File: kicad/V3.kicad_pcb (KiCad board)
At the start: 2 copper layers, 172.9 x 118.3 mm, 51 parts, among them SW1 Slide_Switch_SPDT_P3mm_10x5x1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

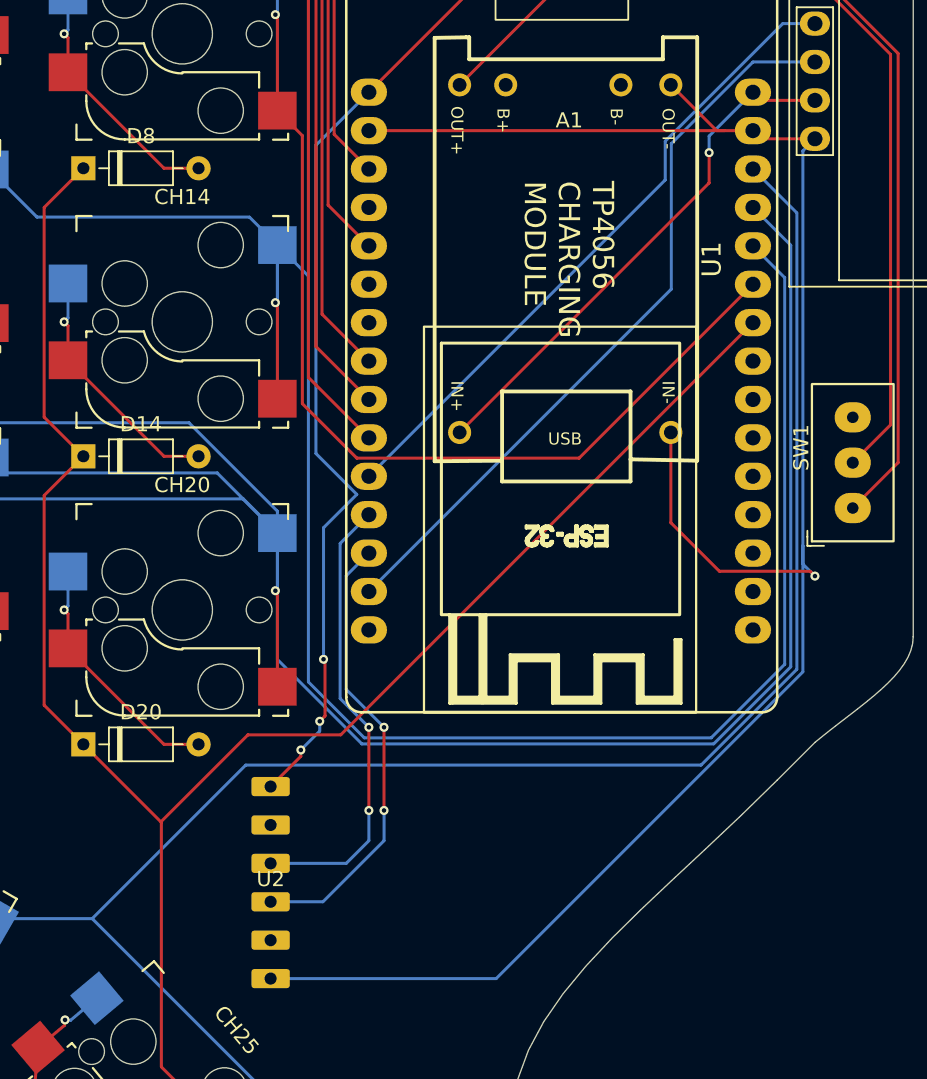
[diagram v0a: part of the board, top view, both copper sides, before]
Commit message: changed uart-hid pinout
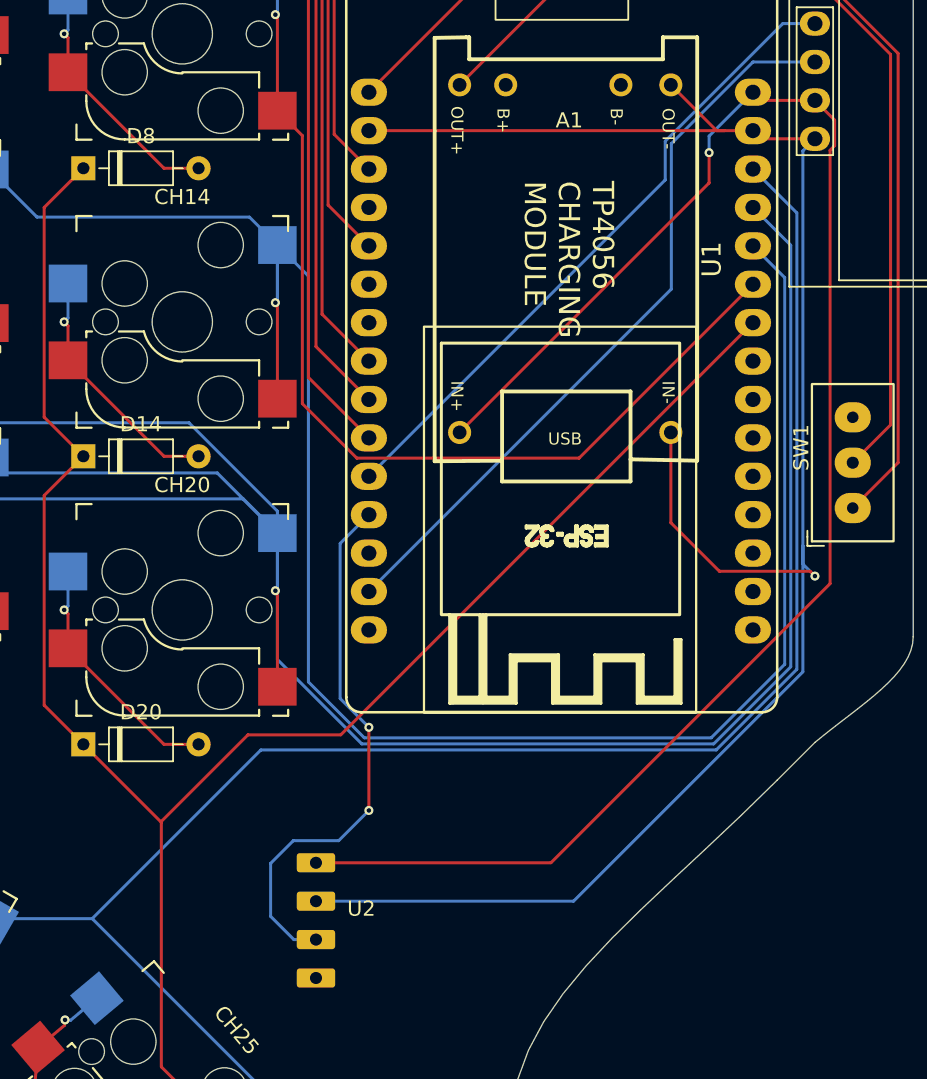
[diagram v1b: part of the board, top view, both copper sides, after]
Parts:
- U2: footprint Library:CH340C_pins -> Library:CH9328
- moved U2 3.63 mm to (194.0, 119.1)
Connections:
- U2 pad 1: -3V3 -> VCC
- U2 pad 2: unconnected-(U2-DTR-Pad2) -> Earth
- U2 pad 4: /TX -> unconnected-(U2-RST-Pad4)
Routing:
- net VCC: track 34.9 -> 109.1 mm
- net -3V3: track 122.3 -> 71.4 mm, vias 3 -> 0
- net /TX: track 29.9 -> 0.00 mm, vias 2 -> 0
- net /RX: track 30.3 -> 36.2 mm
- net Earth: track 133.0 -> 127.9 mm

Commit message: slkscreen
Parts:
- moved U2 7.83 mm to (201.8, 119.2)
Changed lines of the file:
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@@
 		(embedded_fonts no)
 	)
-	(footprint "Library:CH9328"
-		(layer "F.Cu")
-		(at 194 119.08)
-		(property "Reference" "U2"
-			(at 3 -0.58 0)
-			(unlocked yes)
-			(layer "F.SilkS")
-			(effects
-				(font
-					(size 1 1)
-					(thickness 0.1)
-				)
-			)
-		)
-		(property "Value" "~"
-			(at 3 0.92 0)
-			(unlocked yes)
-			(layer "F.Fab")
-			(effects
-				(font
-					(size 1 1)
-					(thickness 0.15)
-				)
-			)
-		)
-		(property "Datasheet" ""
-			(at 0 0 0)
-			(unlocked yes)
-			(layer "F.Fab")
-			(hide yes)
-			(effects
-				(font
-					(size 1 1)
-					(thickness 0.15)
-				)
-			)
-		)
-		(property "Description" ""
-			(at 0 0 0)
-			(unlocked yes)
-			(layer "F.Fab")
-			(hide yes)
-			(effects
-				(font
-					(size 1 1)
-					(thickness 0.15)
-				)
-			)
-		)
-		(sheetname "/")
-		(sheetfile "V3.kicad_sch")
-		(fp_text user "${REFERENCE}"
-			(at 0 2.5 0)
-			(unlocked yes)
-			(layer "F.Fab")
-			(effects
-				(font
-					(size 1 1)
-					(thickness 0.15)
-				)
-			)
-		)
-		(pad "1" thru_hole roundrect
-			(at 0 -3.62)
-			(size 2.54 1.27)
-			(drill 0.8)
-			(layers "*.Cu" "*.Mask")
-			(remove_unused_layers no)
-			(roundrect_rratio 0.15)
-			(net 8 "VCC")
-			(pinfunction "Vcc")
-			(pintype "power_in")
-			(thermal_bridge_angle 45)
-		)
-		(pad "2" thru_hole roundrect
-			(at 0 -1.08)
-			(size 2.54 1.27)
-			(drill 0.8)
-			(layers "*.Cu" "*.Mask")
-			(remove_unused_layers no)
-			(roundrect_rratio 0.15)
-			(net 11 "Earth")
-			(pinfunction "GND")
-			(pintype "power_in")
-			(thermal_bridge_angle 45)
-		)
-		(pad "3" thru_hole roundrect
-			(at 0 1.46)
-			(size 2.54 1.27)
-			(drill 0.8)
-			(layers "*.Cu" "*.Mask")
-			(remove_unused_layers no)
-			(roundrect_rratio 0.15)
-			(net 45 "/RX")
-			(pinfunction "RX")
-			(pintype "input")
-			(thermal_bridge_angle 45)
-		)
-		(pad "4" thru_hole roundrect
-			(at 0 4)
-			(size 2.54 1.27)
-			(drill 0.8)
-			(layers "*.Cu" "*.Mask")
-			(remove_unused_layers no)
-			(roundrect_rratio 0.15)
-			(net 53 "unconnected-(U2-RST-Pad4)")
-			(pinfunction "RST")
-			(pintype "input")
-			(thermal_bridge_angle 45)
-		)
-		(embedded_fonts no)
-	)
 	(footprint "Diode_THT:D_DO-35_SOD27_P7.62mm_Horizontal"
 		(layer "F.Cu")
@@
 		)
 		(embedded_fonts no)
+	)
+	(footprint "Library:CH9328"
+		(layer "F.Cu")
+		(at 201.83262 119.25)
+		(property "Reference" "U2"
+			(at -7.404 -0.7 0)
+			(unlocked yes)
+			(layer "F.SilkS")
+			(effects
+				(font
+					(size 1 1)
+					(thickness 0.1)
+				)
+			)
+		)
+		(property "Value" "~"
+			(at 0 1 0)
+			(unlocked yes)
+			(layer "F.Fab")
+			(effects
+				(font
+					(size 1 1)
+					(thickness 0.15)
+				)
+			)
+		)
+		(property "Datasheet" ""
+			(at 0 0 0)
+			(unlocked yes)
+			(layer "F.Fab")
+			(hide yes)
+			(effects
+				(font
+					(size 1 1)
+					(thickness 0.15)
+				)
+			)
+		)
+		(property "Description" ""
+			(at 0 0 0)
+			(unlocked yes)
+			(layer "F.Fab")
+			(hide yes)
+			(effects
+				(font
+					(size 1 1)
+					(thickness 0.15)
+				)
+			)
+		)
+		(sheetname "/")
+		(sheetfile "V3.kicad_sch")
+		(fp_line
+			(start -10.26124 -10.5)
+			(end -10.26124 10)
+			(stroke
+				(width 0.1)
+				(type default)
+			)
+			(layer "F.SilkS")
+		)
+		(fp_line
+			(start -10.26124 -10.5)
+			(end 15.096 -10.5)
+			(stroke
+				(width 0.1)
+				(type default)
+			)
+			(layer "F.SilkS")
+		)
+		(fp_line
+			(start -10.26124 10)
+			(end 15.096 10)
+			(stroke
+				(width 0.1)
+				(type default)
+			)
+			(layer "F.SilkS")
+		)
+		(fp_line
+			(start 15.096 -10.5)
+			(end 15.096 10)
+			(stroke
+				(width 0.1)
+				(type default)
+			)
+			(layer "F.SilkS")
+		)
+		(fp_rect
+			(start 9.096 -4.5)
+			(end 16.596 4)
+			(stroke
+				(width 0.1)
+				(type default)
+			)
+			(fill no)
+			(layer "F.SilkS")
+		)
+		(fp_text user "Usb"
+			(at 12.096 -2.5 270)
+			(unlocked yes)
+			(layer "F.SilkS")
+			(effects
+				(font
+					(size 1.5 1.5)
+					(thickness 0.3)
+					(bold yes)
+				)
+				(justify left bottom)
+			)
+		)
+		(fp_text user "${REFERENCE}"
+			(at 0 2.5 0)
+			(unlocked yes)
+			(layer "F.Fab")
+			(effects
+				(font
+					(size 1 1)
+					(thickness 0.15)
+				)
+			)
+		)
+		(pad "1" thru_hole roundrect
+			(at -7.404 -3.82)
+			(size 2.54 1.27)
+			(drill 0.8)
+			(layers "*.Cu" "*.Mask")
+			(remove_unused_layers no)
+			(roundrect_rratio 0.15)
+			(net 8 "VCC")
+			(pinfunction "Vcc")
+			(pintype "power_in")
+			(thermal_bridge_angle 45)
+		)
+		(pad "2" thru_hole roundrect
+			(at -7.404 -1.28)
+			(size 2.54 1.27)
+			(drill 0.8)
+			(layers "*.Cu" "*.Mask")
+			(remove_unused_layers no)
+			(roundrect_rratio 0.15)
+			(net 11 "Earth")
+			(pinfunction "GND")
+			(pintype "power_in")
+			(thermal_bridge_angle 45)
+		)
+		(pad "3" thru_hole roundrect
+			(at -7.404 1.26)
+			(size 2.54 1.27)
+			(drill 0.8)
+			(layers "*.Cu" "*.Mask")
+			(remove_unused_layers no)
+			(roundrect_rratio 0.15)
+			(net 45 "/RX")
+			(pinfunction "RX")
+			(pintype "input")
+			(thermal_bridge_angle 45)
+		)
+		(pad "4" thru_hole roundrect
+			(at -7.404 3.8)
+			(size 2.54 1.27)
+			(drill 0.8)
+			(layers "*.Cu" "*.Mask")
+			(remove_unused_layers no)
+			(roundrect_rratio 0.15)
+			(net 53 "unconnected-(U2-RST-Pad4)")
+			(pinfunction "RST")
+			(pintype "input")
+			(thermal_bridge_angle 45)
+		)
+		(embedded_fonts no)

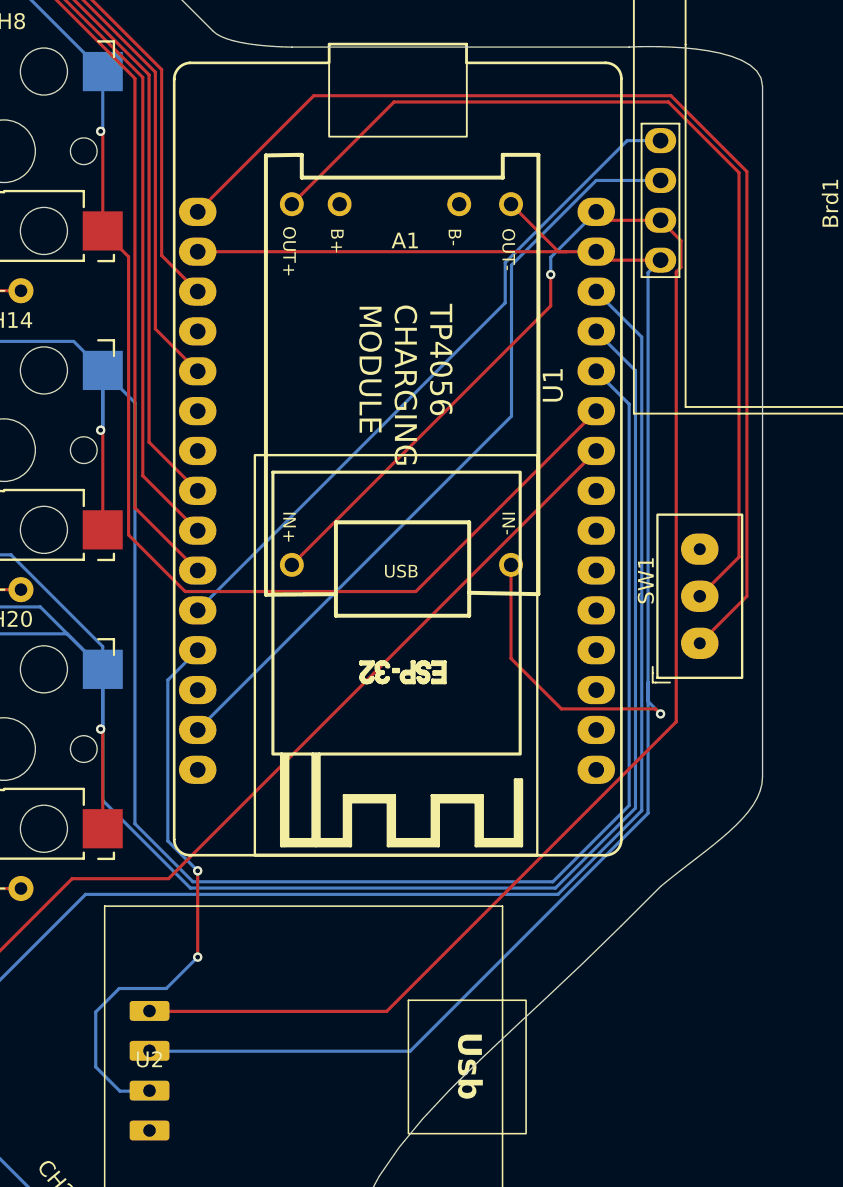
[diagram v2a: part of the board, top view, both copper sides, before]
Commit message: power
shouldnt be charging and discharging now i think
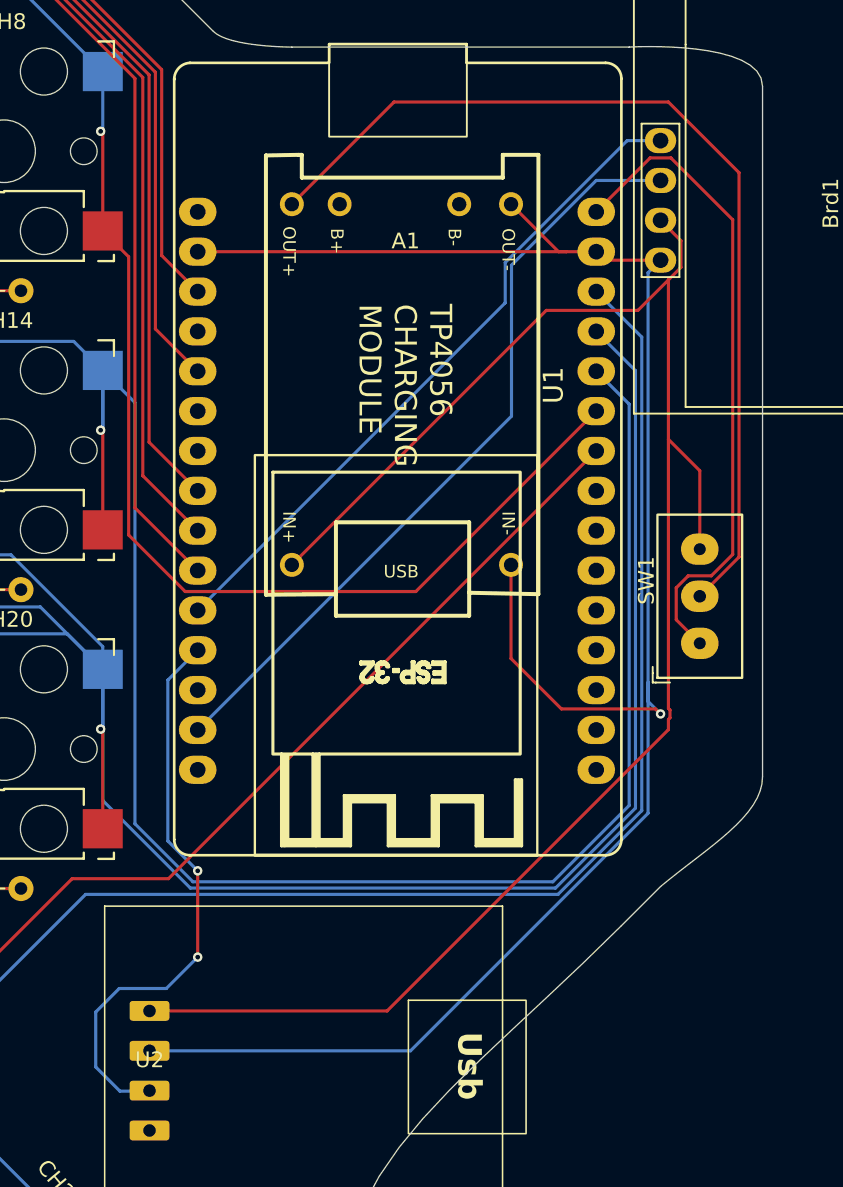
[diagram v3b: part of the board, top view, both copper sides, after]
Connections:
- A1 pad 1: -3V3 -> unconnected-(A1-3.3V-Pad1)
- A1 pad 30: VCC -> /~3v3
- SW1 pad 1: -3V3 -> /~3v3
- SW1 pad 3: unconnected-(SW1-Pad3) -> VCC
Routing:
- net -3V3: track 71.4 -> 0.00 mm
- net /~3v3: track 0.00 -> 41.7 mm
- net VCC: track 109.1 -> 113.3 mm, vias 1 -> 0
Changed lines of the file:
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@@
 	(net 48 "unconnected-(A1-ADC1_CH4{slash}D32-Pad21)")
 	(net 49 "unconnected-(A1-ADC1_CH0{slash}VP-Pad17)")
-	(net 50 "-3V3")
+	(net 50 "unconnected-(A1-3.3V-Pad1)")
 	(net 51 "/SDA")
 	(net 52 "/SCL")
 	(net 53 "unconnected-(U2-RST-Pad4)")
-	(net 54 "unconnected-(SW1-Pad3)")
+	(net 54 "/~3v3")
 	(net 55 "Net-(U1-Out+)")
 	(net 56 "Net-(BT1--)")
@@
 			(layers "*.Cu" "*.Mask")
 			(remove_unused_layers no)
-			(net 50 "-3V3")
+			(net 50 "unconnected-(A1-3.3V-Pad1)")
 			(pinfunction "3.3V")
 			(pintype "power_in")
@@
 			(layers "*.Cu" "*.Mask")
 			(remove_unused_layers no)
-			(net 8 "VCC")
+			(net 54 "/~3v3")
 			(pinfunction "VIN")
 			(pintype "power_in")
@@
 			(layers "*.Cu" "*.Mask")
 			(remove_unused_layers no)
-			(net 50 "-3V3")
+			(net 54 "/~3v3")
 			(pintype "passive")
 		)
@@
 			(layers "*.Cu" "*.Mask")
 			(remove_unused_layers no)
-			(net 54 "unconnected-(SW1-Pad3)")
+			(net 8 "VCC")
 			(pintype "passive")
 		)
@@
 	)
 	(segment
-		(start 228.301 66.341)
-		(end 227 65.04)
+		(start 209.57 115.43)
+		(end 227.5 97.5)
 		(width 0.2)
 		(layer "F.Cu")
@@
 	)
 	(segment
-		(start 228 68.337049)
-		(end 228.301 68.036049)
+		(start 194.42862 115.43)
+		(end 209.57 115.43)
 		(width 0.2)
 		(layer "F.Cu")
@@
 	)
 	(segment
-		(start 223.44 65.04)
-		(end 222.9 64.5)
+		(start 227.5 96.150057)
+		(end 227.5 79)
 		(width 0.2)
 		(layer "F.Cu")
@@
 	)
 	(segment
-		(start 227 65.04)
-		(end 223.44 65.04)
+		(start 219.719 70.781)
+		(end 225.556049 70.781)
 		(width 0.2)
 		(layer "F.Cu")
@@
 	)
 	(segment
-		(start 194 115.46)
-		(end 209.54 115.46)
+		(start 227.5 79)
+		(end 227.5 68.837049)
 		(width 0.2)
 		(layer "F.Cu")
@@
 	)
 	(segment
-		(start 228.301 68.036049)
-		(end 228.301 66.341)
+		(start 229.5 81)
+		(end 227.5 79)
 		(width 0.2)
 		(layer "F.Cu")
@@
 	)
 	(segment
-		(start 209.54 115.46)
-		(end 228 97)
+		(start 227.601 96.748943)
+		(end 227.601 96.251057)
 		(width 0.2)
 		(layer "F.Cu")
@@
 	)
 	(segment
-		(start 220 70.5)
-		(end 220 68.5)
+		(start 227.5 96.849943)
+		(end 227.601 96.748943)
 		(width 0.2)
 		(layer "F.Cu")
@@
 	)
 	(segment
-		(start 228 97)
-		(end 228 68.337049)
+		(start 227.5 97.5)
+		(end 227.5 96.849943)
 		(width 0.2)
 		(layer "F.Cu")
@@
 	)
 	(segment
-		(start 203.5 87)
-		(end 220 70.5)
+		(start 228.301 68.036049)
+		(end 228.301 66.341)
 		(width 0.2)
 		(layer "F.Cu")
 		(net 8)
 	)
-	(via
-		(at 220 68.5)
-		(size 0.6)
-		(drill 0.3)
-		(layers "F.Cu" "B.Cu")
+	(segment
+		(start 227.5 68.837049)
+		(end 228.301 68.036049)
+		(width 0.2)
+		(layer "F.Cu")
 		(net 8)
 	)
 	(segment
-		(start 220 67.4)
-		(end 222.9 64.5)
+		(start 229.5 86)
+		(end 229.5 81)
 		(width 0.2)
-		(layer "B.Cu")
+		(layer "F.Cu")
 		(net 8)
 	)
 	(segment
-		(start 220 68.5)
-		(end 220 67.4)
+		(start 228.301 66.341)
+		(end 227 65.04)
 		(width 0.2)
-		(layer "B.Cu")
+		(layer "F.Cu")
+		(net 8)
+	)
+	(segment
+		(start 227.601 96.251057)
+		(end 227.5 96.150057)
+		(width 0.2)
+		(layer "F.Cu")
+		(net 8)
+	)
+	(segment
+		(start 225.556049 70.781)
+		(end 227.5 68.837049)
+		(width 0.2)
+		(layer "F.Cu")
+		(net 8)
+	)
+	(segment
+		(start 203.5 87)
+		(end 219.719 70.781)
+		(width 0.2)
+		(layer "F.Cu")
 		(net 8)
 	)
@@
 	)
 	(segment
-		(start 226.203 95.703)
-		(end 227 96.5)
+		(start 226.203 102.8322)
+		(end 226.203 94.5)
 		(width 0.2)
 		(layer "B.Cu")
@@
 	)
 	(segment
-		(start 226.203 68.377)
-		(end 227 67.58)
+		(start 226.203 95.703)
+		(end 227 96.5)
 		(width 0.2)
 		(layer "B.Cu")
@@
 	)
 	(segment
-		(start 226.203 102.8322)
-		(end 211.0352 118)
+		(start 194.42862 117.97)
+		(end 211.0652 117.97)
 		(width 0.2)
 		(layer "B.Cu")
@@
 	)
 	(segment
-		(start 226.203 102.8322)
-		(end 226.203 94.5)
+		(start 226.203 68.377)
+		(end 227 67.58)
 		(width 0.2)
 		(layer "B.Cu")
@@
 	)
 	(segment
-		(start 226.203 94.5)
-		(end 226.203 68.377)
+		(start 211.0652 117.97)
+		(end 226.203 102.8322)
 		(width 0.2)
 		(layer "B.Cu")
@@
 	)
 	(segment
-		(start 211.0352 118)
-		(end 194 118)
+		(start 226.203 94.5)
+		(end 226.203 68.377)
 		(width 0.2)
 		(layer "B.Cu")
@@
 	)
 	(segment
-		(start 195.5 114)
-		(end 197.5 112)
+		(start 191 119)
+		(end 192.54 120.54)
 		(width 0.2)
 		(layer "B.Cu")
@@
 	)
 	(segment
-		(start 192.54 120.54)
-		(end 191 119)
+		(start 195.5 114)
+		(end 197.5 112)
 		(width 0.2)
 		(layer "B.Cu")
@@
 	)
 	(segment
-		(start 204.901 57.099)
-		(end 227.6661 57.099)
-		(width 0.2)
-		(layer "F.Cu")
-		(net 50)
-	)
-	(segment
-		(start 232.5 61.9329)
-		(end 232.5 89)
-		(width 0.2)
-		(layer "F.Cu")
-		(net 50)
-	)
-	(segment
-		(start 227.6661 57.099)
-		(end 232.5 61.9329)
-		(width 0.2)
-		(layer "F.Cu")
-		(net 50)
-	)
-	(segment
-		(start 232.5 89)
-		(end 229.5 92)
-		(width 0.2)
-		(layer "F.Cu")
-		(net 50)
-	)
-	(segment
-		(start 197.5 64.5)
-		(end 204.901 57.099)
-		(width 0.2)
-		(layer "F.Cu")
-		(net 50)
-	)
-	(segment
 		(start 217.099 67.73543)
 		(end 224.87443 59.96)
@@
 	)
 	(segment
+		(start 227.999 88.461108)
+		(end 228.761108 87.699)
+		(width 0.2)
+		(layer "F.Cu")
+		(net 54)
+	)
+	(segment
+		(start 229.5 92)
+		(end 227.999 90.499)
+		(width 0.2)
+		(layer "F.Cu")
+		(net 54)
+	)
+	(segment
+		(start 226.339 61.061)
+		(end 222.9 64.5)
+		(width 0.2)
+		(layer "F.Cu")
+		(net 54)
+	)
+	(segment
+		(start 228.761108 87.699)
+		(end 230.2339 87.699)
+		(width 0.2)
+		(layer "F.Cu")
+		(net 54)
+	)
+	(segment
+		(start 231.599 86.3339)
+		(end 231.599 65.003951)
+		(width 0.2)
+		(layer "F.Cu")
+		(net 54)
+	)
+	(segment
+		(start 227.999 90.499)
+		(end 227.999 88.461108)
+		(width 0.2)
+		(layer "F.Cu")
+		(net 54)
+	)
+	(segment
+		(start 227.656049 61.061)
+		(end 226.339 61.061)
+		(width 0.2)
+		(layer "F.Cu")
+		(net 54)
+	)
+	(segment
+		(start 230.2339 87.699)
+		(end 231.599 86.3339)
+		(width 0.2)
+		(layer "F.Cu")
+		(net 54)
+	)
+	(segment
+		(start 231.599 65.003951)
+		(end 227.656049 61.061)
+		(width 0.2)
+		(layer "F.Cu")
+		(net 54)
+	)
+	(segment
 		(start 203.5 64.013)
 		(end 210.013 57.5)
@@
 	)
 	(segment
-		(start 232 86.5)
-		(end 229.5 89)
+		(start 229.5 89)
+		(end 232 86.5)
 		(width 0.2)
 		(layer "F.Cu")

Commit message: positoins
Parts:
- moved D22 6.26 mm to (63.9, 75.7), turned to 5 degrees
- moved CH22 5.88 mm to (69.6, 66.3), turned to 5 degrees
- moved D15 5.09 mm to (85.9, 112.1), turned to 5 degrees
- moved D3 4.65 mm to (82.5, 74.1), turned to 5 degrees
- moved D9 4.58 mm to (84.2, 93.1), turned to 5 degrees
- moved CH3 4.35 mm to (88.3, 64.7), turned to 5 degrees
- moved CH15 4.25 mm to (91.6, 102.6), turned to 5 degrees
- moved CH9 3.97 mm to (89.9, 83.7), turned to 5 degrees
- moved D16 3.68 mm to (104.8, 110.4), turned to 5 degrees
- moved D4 3.05 mm to (101.5, 72.4), turned to 5 degrees
- moved D10 2.95 mm to (103.2, 91.4), turned to 5 degrees
- moved CH4 2.92 mm to (107.3, 63.0), turned to 5 degrees
- moved CH16 2.76 mm to (110.6, 101.0), turned to 5 degrees
- moved CH10 2.31 mm to (108.9, 82.0), turned to 5 degrees
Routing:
- net /Row2: track 281.8 -> 267.6 mm
- net /Col1: track 193.0 -> 196.6 mm
- net /Col2: track 217.3 -> 220.9 mm
- net /Row4: track 339.7 -> 336.2 mm
- net /Row1: track 225.1 -> 228.1 mm
- net /Row3: track 308.8 -> 309.4 mm
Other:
- board size 172.9 x 118.3 mm -> 175.1 x 118.3 mm

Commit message: wiring
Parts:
- moved CH15 0.43 mm to (91.2, 102.6)
- moved CH22 0.43 mm to (69.2, 66.3)
- moved CH3 0.43 mm to (87.9, 64.7)
- moved CH4 0.43 mm to (106.8, 63.0)
- moved D9 0.43 mm to (83.8, 93.1)
- moved CH9 0.43 mm to (89.5, 83.7)
- moved D15 0.43 mm to (85.4, 112.1)
- moved D22 0.43 mm to (63.5, 75.7)
- moved D4 0.43 mm to (101.1, 72.4)
- moved CH10 0.43 mm to (108.5, 82.0)
- moved CH16 0.43 mm to (110.2, 101.0)
- moved D10 0.43 mm to (102.8, 91.4)
- moved D16 0.43 mm to (104.4, 110.4)
- moved D3 0.43 mm to (82.1, 74.1)
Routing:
- net /Col1: track 196.6 -> 200.2 mm
- net /Row1: track 228.1 -> 227.6 mm
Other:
- board size 175.1 x 118.3 mm -> 175.6 x 118.3 mm
